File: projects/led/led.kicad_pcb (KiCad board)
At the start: 2 copper layers, 12 x 9.2 mm, 3 parts, among them J1 Conn_01x02

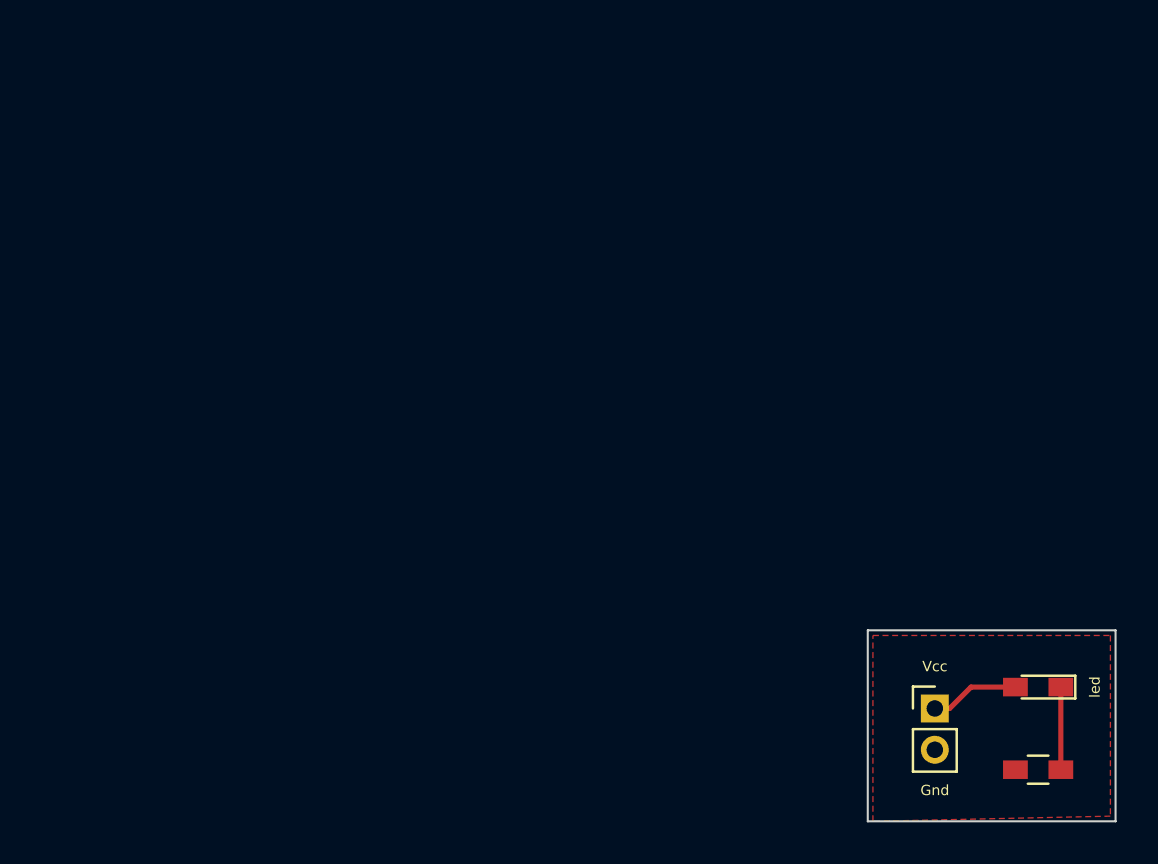
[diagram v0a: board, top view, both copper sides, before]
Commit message: Add new led project example for pcb milling
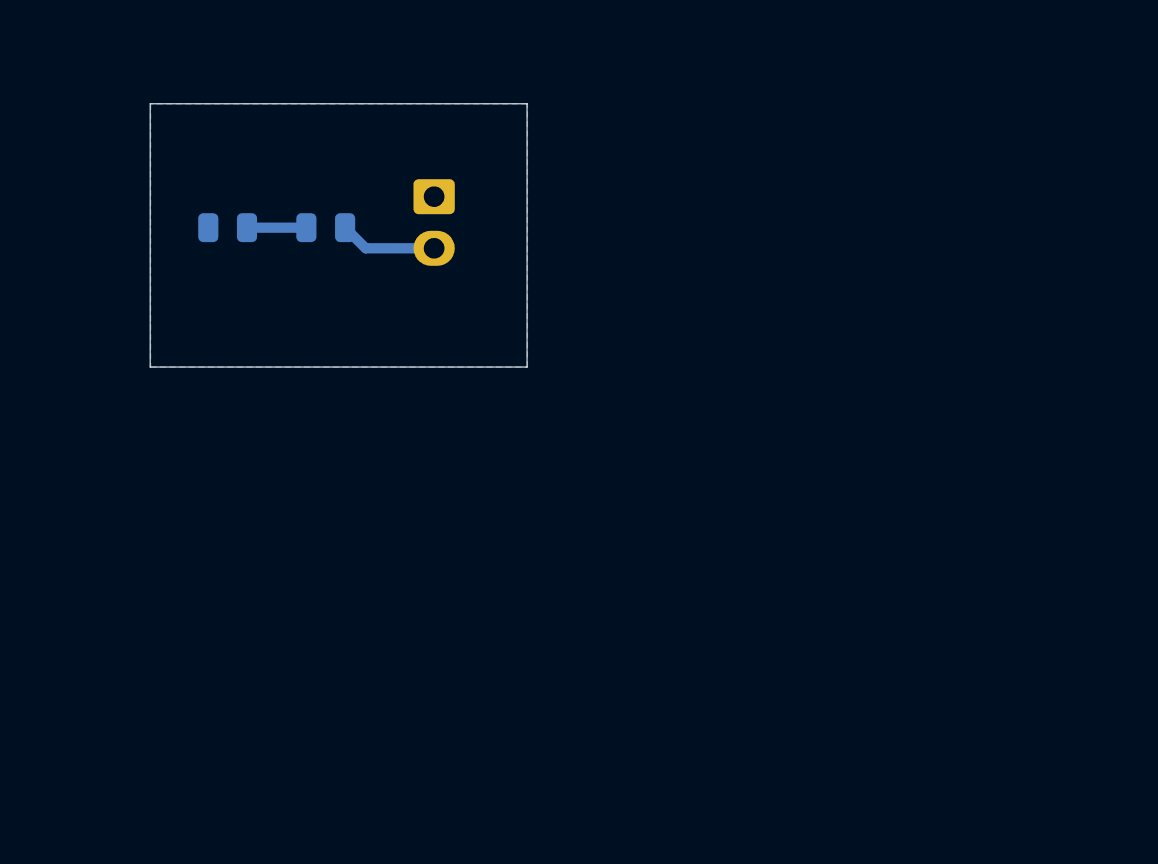
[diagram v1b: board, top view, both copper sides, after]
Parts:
- removed led: LED, LEDs:LED_0603_HandSoldering
- added D1: LED, LED_SMD:LED_0805_2012Metric, B.Cu at (123.8, 68.5)
- J1: value Conn_01x02 -> Conn_01x02_Pin; footprint Pin_Headers:Pin_Header_Straight_1x02_Pitch2.00mm -> Connector_JST:JST_EH_B2B-EH-A_1x02_P2.50mm_Vertical; moved to B.Cu
- R1: footprint Resistors_SMD:R_0603_HandSoldering -> LED_SMD:LED_0805_2012Metric; moved to B.Cu
- moved R1 43.4 mm to (128.5, 68.5), turned to 0 degrees
- moved J1 34.7 mm to (133.8, 67.0), turned to -90 degrees
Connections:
- J1 pad 1: VCC -> GND
- J1 pad 2: GND -> VCC
- R1 pad 2: GND -> VCC
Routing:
- net Net-(D1-A): track 4.00 -> 2.88 mm
- added copper zone on B.Cu, net GND
- removed copper zone on F.Cu, net GND
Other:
- board size 12 x 9.2 mm -> 18.2 x 12.8 mm
- net class Default removed
- board text removed: "Gnd"
- board text removed: "Vcc"

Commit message: add more
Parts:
- added H1: MountingHole, MountingHole:MountingHole_2.2mm_M2_DIN965, B.Cu at (118.8, 63.0)
- added H2: MountingHole, MountingHole:MountingHole_2.2mm_M2_DIN965, B.Cu at (138.5, 76.5)
- J1: moved to F.Cu
- moved D1 1.93 mm to (122.0, 69.2)
- moved R1 1.54 mm to (127.2, 69.2)
- moved J1 1.38 mm to (134.9, 67.8)
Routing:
- net VCC: track 4.73 -> 7.23 mm
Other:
- board size 18.2 x 12.8 mm -> 27.5 x 20.5 mm
